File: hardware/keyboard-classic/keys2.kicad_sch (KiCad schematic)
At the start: 58 parts, among them SW1 RT Arrow, SW10 Bracket_Open, SW11 6, SW12 Y, SW13 Return, SW14 Dash, SW15 5, SW16 T, SW18 Colon, SW19 4, SW2 LT Arrow, SW20 R, SW21 O, SW22 0, SW23 3, SW24 E, SW25 L, SW26 9, SW27 2, SW28 W, SW29 Period, SW3 Tilde, SW30 8, SW31 1, SW4 I, SW5 Repeat, SW6 Bracket_Close, SW7 7, SW8 U

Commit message: Add some mounting hardware
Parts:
- D11, D12, D13, D14, D15, D16, D17, D19, D2, D20, D21, D22, D23, D24, D25, D26, D27, D28, D29, D3, D30, D31, D32, D4, D5, D6, D7, D8, D9: Manufacturer PN (none) -> MMBD914LT3G
- SW1: symbol Switch:SW_Push -> unikbd:SW Cherry MX/Futaba 1U Style A; Allow Substitution (none) -> Yes; Class (none) -> If applicable; Component Type (none) -> Switch; Component Value (none) -> Key; Manufacturer Futaba(1) or Cherry(2) -> Cherry; Manufacturer Link (none) -> https://www.cherrymx.de/en/cherry-mx/mx-original/mx-black.h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; Manufacturer PN (none) -> MX1A-11NN; Manufacturer Part Number (1) MD4-PCS (2) Cherry MX or clone -> MX1A-11NN; Material (none) -> If applicable; Number of Pins (none) -> 2; Power Rating (none) -> 10 mA; RoHS (none) -> Yes; RoHS Document Link (none) -> https://www.mouser.com/catalog/additional/Cherry_Electrical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; Standards Version (none) -> 1.1; Temp (Operating) (none) -> -40C/+170C; Temp (Soldering) (none) -> If applicable; Temp Coeff. (none) -> If applicable; Tolerance (none) -> If applicable; Tracking (none) -> No
- SW10, SW11, SW12, SW14, SW15, SW16, SW18, SW19, SW2, SW20, SW21, SW22, SW23, SW24, SW25, SW26, SW27, SW28, SW29, SW3, SW30, SW31, SW4, SW5, SW6, SW7, SW8: symbol Switch:SW_Push -> unikbd:SW Cherry MX/Futaba 1U Style A; Allow Substitution (none) -> Yes; Class (none) -> If applicable; Component Type (none) -> Switch; Component Value (none) -> Key; Manufacturer (none) -> Cherry; Manufacturer Link (none) -> https://www.cherrymx.de/en/cherry-mx/mx-original/mx-black.h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; Manufacturer PN (none) -> MX1A-11NN; Manufacturer Part Number (none) -> MX1A-11NN; Material (none) -> If applicable; Number of Pins (none) -> 2; Power Rating (none) -> 10 mA; RoHS (none) -> Yes; RoHS Document Link (none) -> https://www.mouser.com/catalog/additional/Cherry_Electrical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; Standards Version (none) -> 1.1; Temp (Operating) (none) -> -40C/+170C; Temp (Soldering) (none) -> If applicable; Temp Coeff. (none) -> If applicable; Tolerance (none) -> If applicable; Tracking (none) -> No
- SW13: symbol Switch:SW_Push -> unikbd:SW Cherry MX/Futaba 1U Style A; Allow Substitution (none) -> Yes; BOM Comment (none) -> 1.5U; Class (none) -> If applicable; Component Type (none) -> Switch; Component Value (none) -> Key; Manufacturer (none) -> Cherry; Manufacturer Link (none) -> https://www.cherrymx.de/en/cherry-mx/mx-original/mx-black.h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; Manufacturer PN (none) -> MX1A-11NN; Manufacturer Part Number (none) -> MX1A-11NN; Material (none) -> If applicable; Number of Pins (none) -> 2; Power Rating (none) -> 10 mA; RoHS (none) -> Yes; RoHS Document Link (none) -> https://www.mouser.com/catalog/additional/Cherry_Electrical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; Standards Version (none) -> 1.1; Temp (Operating) (none) -> -40C/+170C; Temp (Soldering) (none) -> If applicable; Temp Coeff. (none) -> If applicable; Tolerance (none) -> If applicable; Tracking (none) -> No

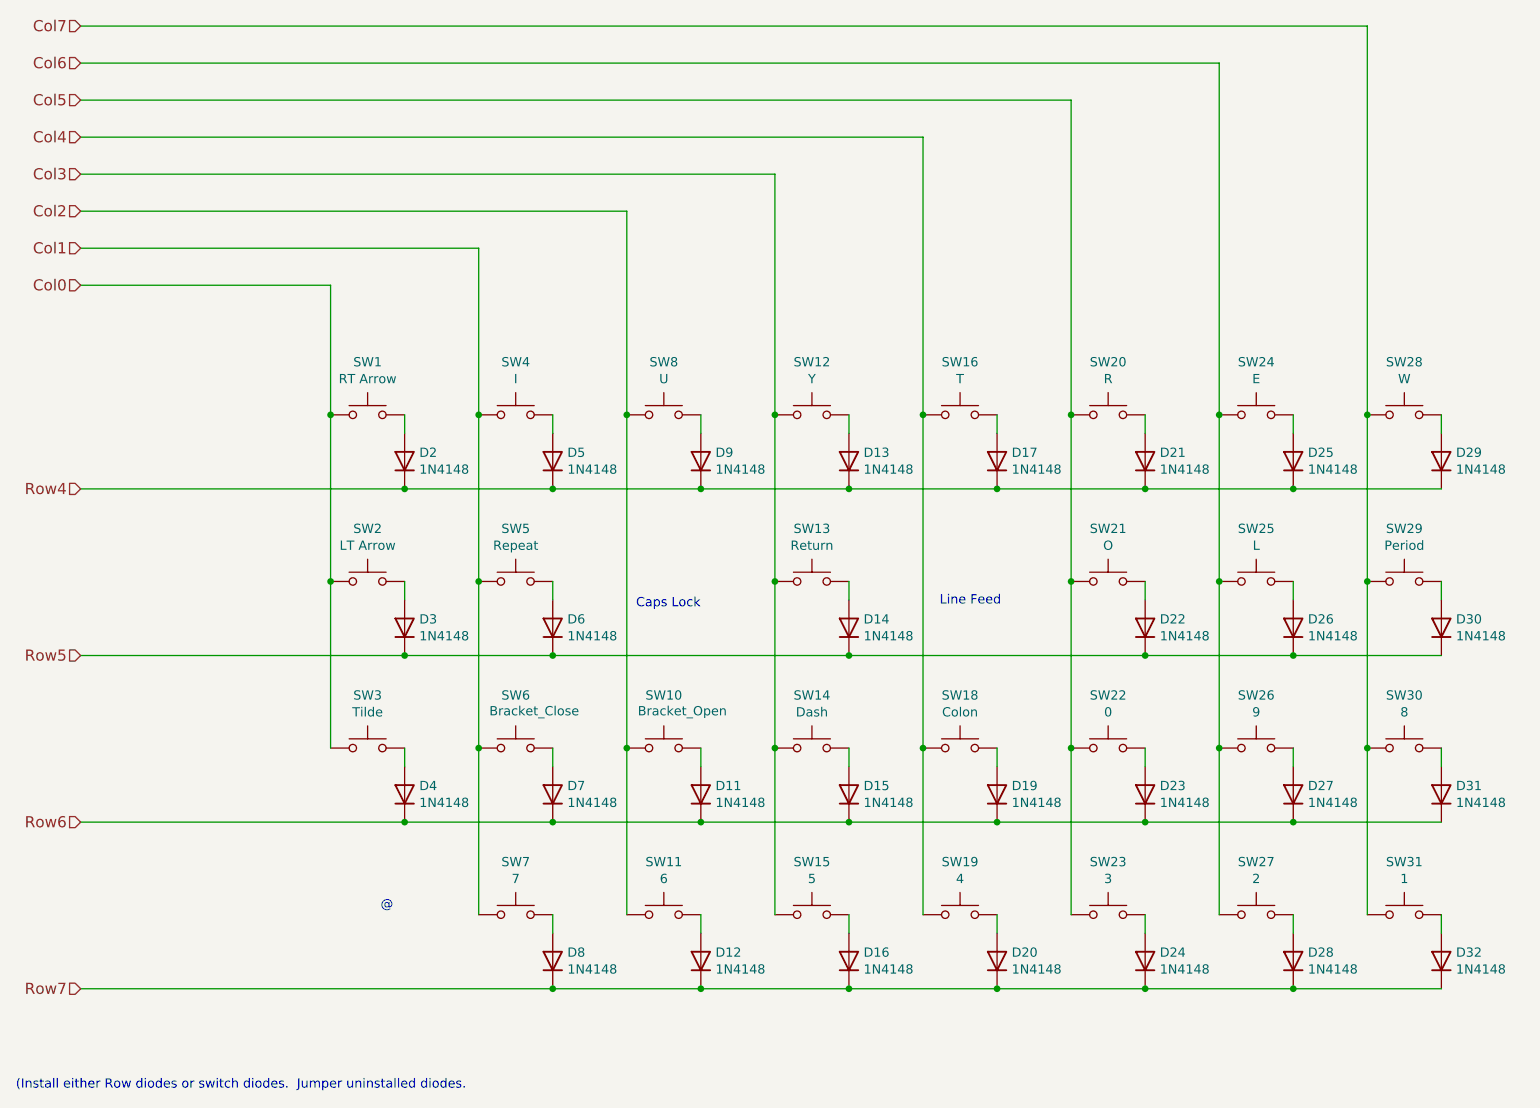
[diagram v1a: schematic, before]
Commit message: Update to include mounting hardware
- Fix all components to include full information including BOM
information

- Include all mounting hardware in components List

- fix schematic to align on 0.1" grid.
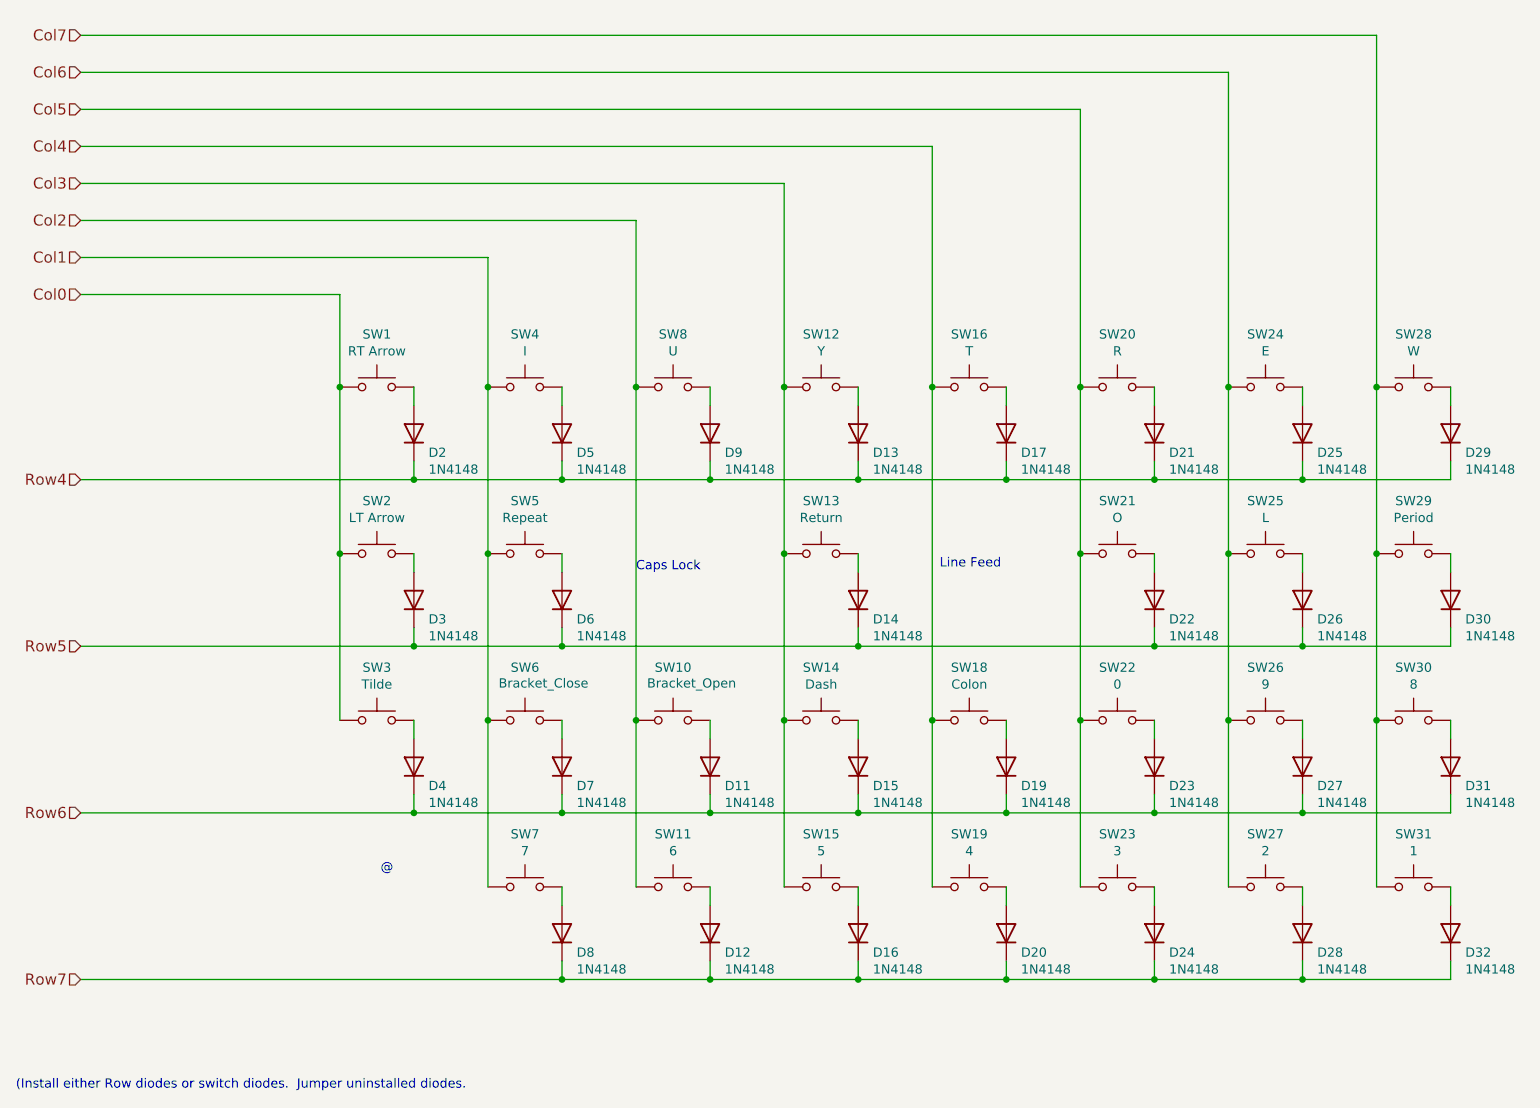
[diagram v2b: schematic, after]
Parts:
- D11, D12, D13, D14, D15, D16, D17, D19, D2, D20, D21, D22, D23, D24, D25, D26, D27, D28, D29, D3, D30, D31, D32, D4, D5, D6, D7, D8, D9: Allow Substitution (none) -> Yes; BOM Comment (none) -> Either SMT or Through-Hole part (1n914 or 1n4148) is fitted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; Class (none) -> If applicable; Component Type (none) -> Diode; Component Value (none) -> 19N14/MMBD914; Fitted YES -> Yes; Manufacturer ON Semiconductor -> Diodes, Inc.; Manufacturer Link (none) -> https://www.diodes.com/part/view/MMBD914; Manufacturer PN MMBD914LT3G -> MMBD914-7-F; Material (none) -> If applicable; Number of Pins (none) -> 3; Package Type (none) -> SOT3-3; Power Rating (none) -> 350 mW / 200 mA; RoHS (none) -> Yes; RoHS Document Link (none) -> https://www.diodes.com/assets/Quality-Reliability-Docs/Mast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; Standards Version (none) -> 1.1; Temp (Operating) (none) -> -65C/150C; Temp (Soldering) (none) -> If applicable; Temp (Storage) (none) -> If applicable; Temp Coeff. (none) -> If applicable; Tolerance (none) -> If applicable; Tracking (none) -> No
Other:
- moved on the sheet: D11, D12, D13, D14, D15, D16, D17, D19, D2, D20, D21, D22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
